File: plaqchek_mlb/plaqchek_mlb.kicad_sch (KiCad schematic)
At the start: 26 parts, among them J1 Conn_01x05, J2 Conn_01x04, J3 Conn_01x02, J4 Conn_01x16, J5 Conn_01x04, SW1 SW_SPST, SW2 SW_Push, SW3 SW_Push, U1 DHT11

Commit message: finish schematic
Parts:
- removed J1: Conn_01x05, symbol Connector_Generic:Conn_01x05
- added C2: 0.1uF, symbol Device:C_Small
- added C3: 10uF, symbol Device:C_Small
- added D1, D2, D3: LED, symbol Device:LED
- added J1: Conn_01x04, symbol Connector_Generic:Conn_01x04
- added R11, R12, R9: 330R, symbol Device:R_Small_US
- R1, R2, R3: value 0 -> 0R
- R10, R33, R34, R8: value 10k -> 10kR
- R31, R7: value 1kΩ -> 1kR
- R4, R5, R6: value 0Ω -> 0R
- U1: value DHT11 -> DHT22
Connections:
- net UNUSED_D2 is gone; now on net UNUSED_D4: J4.5 (Pin_5)
- net UNUSED_D6 is gone; now on net UNUSED_A3: J4.8 (Pin_8)
- net +12V: now also C1.1
- net +3V3: now also C2.1, C3.1; no longer C1.1
- net GND: now also J4.14 (Pin_14), J4.15 (Pin_15), C2.2, C3.2, D1.1 (K), D2.1 (K), D3.1 (K), J1.4 (Pin_4)
- net LED1: now also R9.2
- net LED2: now also R11.2
- net LED3: now also R12.2
- net SPI_5V_ADC_CS: now also J1.1 (Pin_1)
- net SPI_5V_ADC_MISO: now also J1.2 (Pin_2)
- net SPI_5V_ADC_SCLK: now also J1.3 (Pin_3)
- net UNUSED_A3: no longer J4.10 (Pin_10)
- net UNUSED_A6: now also J4.9 (Pin_9); no longer J4.11 (Pin_11)
- net UNUSED_A7: now also J4.10 (Pin_10); no longer J4.12 (Pin_12)
- net UNUSED_AREF: now also J4.11 (Pin_11); no longer J4.13 (Pin_13)
- net UNUSED_D11: now also J4.7 (Pin_7); no longer J4.9 (Pin_9)
- net UNUSED_D4: no longer J4.6 (Pin_6)
- net UNUSED_D5: now also J4.6 (Pin_6); no longer J4.7 (Pin_7)
- net UNUSED_RESET_L_1: now also J4.12 (Pin_12); no longer J4.14 (Pin_14)
- net UNUSED_RESET_L_2: now also J4.13 (Pin_13); no longer J4.15 (Pin_15)
- new net: D2.2 (A), R11.1
- new net: D3.2 (A), R12.1
- new net: D1.2 (A), R9.1
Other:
- moved on the sheet: C1, U1

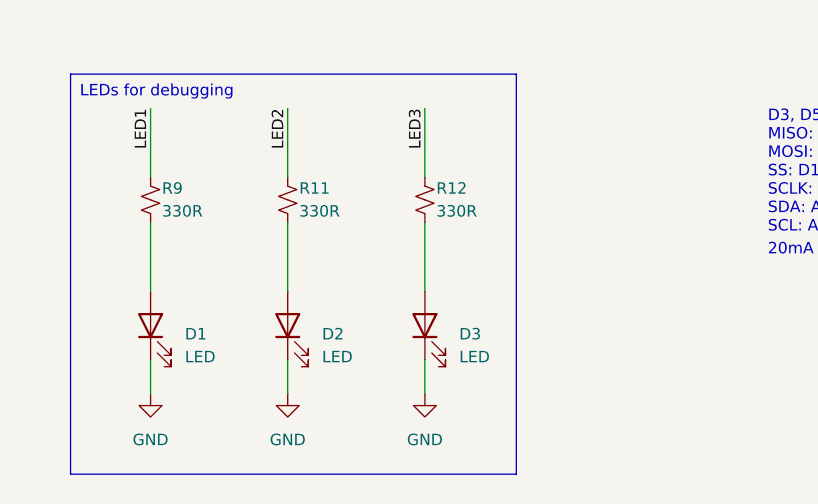
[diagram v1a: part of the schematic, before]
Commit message: more footprints and some value fixes
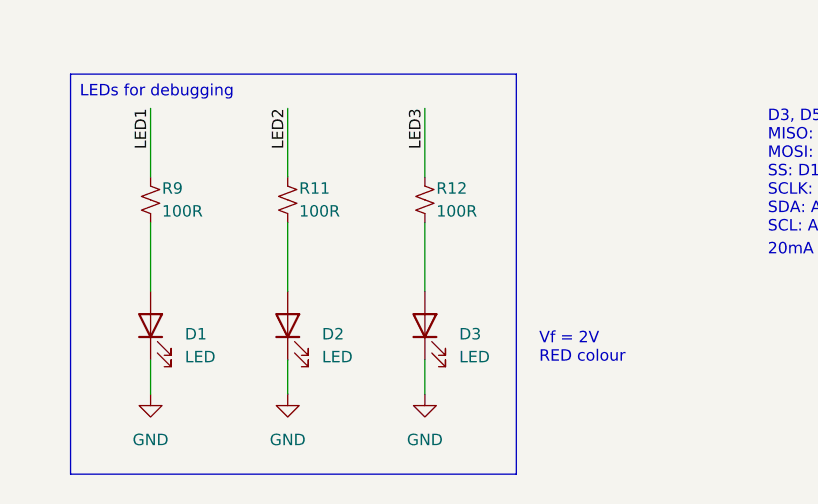
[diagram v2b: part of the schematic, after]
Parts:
- C1, C2, C3, C4, C5: footprint (none) -> Capacitor_SMD:C_0603_1608Metric_Pad1.08x0.95mm_HandSolder
- D1, D2, D3: footprint (none) -> LED_SMD:LED_0805_2012Metric_Pad1.15x1.40mm_HandSolder
- J1, J2, J5: footprint (none) -> Connector_PinHeader_2.54mm:PinHeader_1x04_P2.54mm_Vertical
- J3, JP1: footprint (none) -> Connector_PinHeader_2.54mm:PinHeader_1x02_P2.54mm_Vertical
- J4: footprint (none) -> Connector_PinHeader_2.54mm:PinHeader_1x16_P2.54mm_Vertical
- R1, R10, R2, R3, R31, R33, R34, R4, R5, R6, R7, R8: footprint (none) -> Resistor_SMD:R_0201_0603Metric_Pad0.64x0.40mm_HandSolder
- R11, R12, R9: value 330R -> 100R; footprint (none) -> Resistor_SMD:R_0201_0603Metric_Pad0.64x0.40mm_HandSolder
- SW1, SW2, SW3: footprint (none) -> Button_Switch_THT:SW_PUSH_6mm_H13mm
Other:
- note added: "Vf = 2V RED colour"
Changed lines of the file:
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@@
+    (effects (font (size 1.27 1.27)) (justify left bottom))
+  )
+  (text "Vf = 2V\nRED colour\n\n" (at 73.66 182.88 0)
     (effects (font (size 1.27 1.27)) (justify left bottom))
   )
@@
       (effects (font (size 1.27 1.27)) (justify left))
     )
-    (property "Footprint" "" (at 83.82 39.37 0)
+    (property "Footprint" "Capacitor_SMD:C_0603_1608Metric_Pad1.08x0.95mm_HandSolder" (at 83.82 39.37 0)
       (effects (font (size 1.27 1.27)) hide)
     )
@@
       (effects (font (size 1.27 1.27)))
     )
-    (property "Footprint" "" (at 63.5 72.39 0)
+    (property "Footprint" "Connector_PinHeader_2.54mm:PinHeader_1x02_P2.54mm_Vertical" (at 63.5 72.39 0)
       (effects (font (size 1.27 1.27)) hide)
     )
@@
       (effects (font (size 1.27 1.27)) (justify left))
     )
-    (property "Footprint" "" (at 232.41 144.78 0)
+    (property "Footprint" "Connector_PinHeader_2.54mm:PinHeader_1x04_P2.54mm_Vertical" (at 232.41 144.78 0)
       (effects (font (size 1.27 1.27)) hide)
     )
@@
       (effects (font (size 1.27 1.27)) (justify left))
     )
-    (property "Footprint" "" (at 167.64 30.48 0)
+    (property "Footprint" "Button_Switch_THT:SW_PUSH_6mm_H13mm" (at 167.64 30.48 0)
       (effects (font (size 1.27 1.27)) hide)
     )
@@
       (effects (font (size 1.27 1.27)) (justify right))
     )
-    (property "Value" "330R" (at 46.99 163.83 0)
-      (effects (font (size 1.27 1.27)) (justify right))
-    )
-    (property "Footprint" "" (at 45.72 162.56 0)
+    (property "Value" "100R" (at 46.99 163.83 0)
+      (effects (font (size 1.27 1.27)) (justify right))
+    )
+    (property "Footprint" "Resistor_SMD:R_0201_0603Metric_Pad0.64x0.40mm_HandSolder" (at 45.72 162.56 0)
       (effects (font (size 1.27 1.27)) hide)
     )
@@
       (effects (font (size 1.27 1.27)) (justify right))
     )
-    (property "Footprint" "" (at 194.31 138.43 0)
+    (property "Footprint" "Resistor_SMD:R_0201_0603Metric_Pad0.64x0.40mm_HandSolder" (at 194.31 138.43 0)
       (effects (font (size 1.27 1.27)) hide)
     )
@@
       (effects (font (size 1.27 1.27)) (justify left))
     )
-    (property "Footprint" "" (at 72.39 39.37 0)
+    (property "Footprint" "Capacitor_SMD:C_0603_1608Metric_Pad1.08x0.95mm_HandSolder" (at 72.39 39.37 0)
       (effects (font (size 1.27 1.27)) hide)
     )
@@
       (effects (font (size 1.27 1.27)) (justify right))
     )
-    (property "Footprint" "" (at 60.96 176.53 0)
+    (property "Footprint" "LED_SMD:LED_0805_2012Metric_Pad1.15x1.40mm_HandSolder" (at 60.96 176.53 0)
       (effects (font (size 1.27 1.27)) hide)
     )
@@
       (effects (font (size 1.27 1.27)) (justify right))
     )
-    (property "Footprint" "" (at 41.91 99.06 0)
+    (property "Footprint" "Resistor_SMD:R_0201_0603Metric_Pad0.64x0.40mm_HandSolder" (at 41.91 99.06 0)
       (effects (font (size 1.27 1.27)) hide)
     )
@@
       (effects (font (size 1.27 1.27)))
     )
-    (property "Footprint" "" (at 204.47 119.38 0)
+    (property "Footprint" "Button_Switch_THT:SW_PUSH_6mm_H13mm" (at 204.47 119.38 0)
       (effects (font (size 1.27 1.27)) hide)
     )
@@
       (effects (font (size 1.27 1.27)) (justify right))
     )
-    (property "Footprint" "" (at 58.42 119.38 0)
+    (property "Footprint" "Resistor_SMD:R_0201_0603Metric_Pad0.64x0.40mm_HandSolder" (at 58.42 119.38 0)
       (effects (font (size 1.27 1.27)) hide)
     )
@@
       (effects (font (size 1.27 1.27)) (justify right))
     )
-    (property "Footprint" "" (at 181.61 119.38 0)
+    (property "Footprint" "Resistor_SMD:R_0201_0603Metric_Pad0.64x0.40mm_HandSolder" (at 181.61 119.38 0)
       (effects (font (size 1.27 1.27)) hide)
     )
@@
       (effects (font (size 1.27 1.27)) (justify right))
     )
-    (property "Footprint" "" (at 161.29 116.84 0)
+    (property "Footprint" "Resistor_SMD:R_0201_0603Metric_Pad0.64x0.40mm_HandSolder" (at 161.29 116.84 0)
       (effects (font (size 1.27 1.27)) hide)
     )
@@
       (effects (font (size 1.27 1.27)))
     )
-    (property "Footprint" "" (at 33.02 39.37 0)
+    (property "Footprint" "Connector_PinHeader_2.54mm:PinHeader_1x04_P2.54mm_Vertical" (at 33.02 39.37 0)
       (effects (font (size 1.27 1.27)) hide)
     )
@@
       (effects (font (size 1.27 1.27)) (justify right))
     )
-    (property "Footprint" "" (at 81.28 132.08 0)
+    (property "Footprint" "Resistor_SMD:R_0201_0603Metric_Pad0.64x0.40mm_HandSolder" (at 81.28 132.08 0)
       (effects (font (size 1.27 1.27)) hide)
     )
@@
       (effects (font (size 1.27 1.27)) (justify right))
     )
-    (property "Footprint" "" (at 162.56 41.91 0)
+    (property "Footprint" "Resistor_SMD:R_0201_0603Metric_Pad0.64x0.40mm_HandSolder" (at 162.56 41.91 0)
       (effects (font (size 1.27 1.27)) hide)
     )
@@
       (effects (font (size 1.27 1.27)) (justify right))
     )
-    (property "Value" "330R" (at 62.23 163.83 0)
-      (effects (font (size 1.27 1.27)) (justify right))
-    )
-    (property "Footprint" "" (at 60.96 162.56 0)
+    (property "Value" "100R" (at 62.23 163.83 0)
+      (effects (font (size 1.27 1.27)) (justify right))
+    )
+    (property "Footprint" "Resistor_SMD:R_0201_0603Metric_Pad0.64x0.40mm_HandSolder" (at 60.96 162.56 0)
       (effects (font (size 1.27 1.27)) hide)
     )
@@
       (effects (font (size 1.27 1.27)) (justify left))
     )
-    (property "Footprint" "" (at 71.12 80.01 0)
+    (property "Footprint" "Capacitor_SMD:C_0603_1608Metric_Pad1.08x0.95mm_HandSolder" (at 71.12 80.01 0)
       (effects (font (size 1.27 1.27)) hide)
     )
@@
       (effects (font (size 1.27 1.27)) (justify left))
     )
-    (property "Footprint" "" (at 190.5 30.48 0)
+    (property "Footprint" "Button_Switch_THT:SW_PUSH_6mm_H13mm" (at 190.5 30.48 0)
       (effects (font (size 1.27 1.27)) hide)
     )
@@
       (effects (font (size 1.27 1.27)) (justify left))
     )
-    (property "Footprint" "" (at 80.01 80.01 0)
+    (property "Footprint" "Capacitor_SMD:C_0603_1608Metric_Pad1.08x0.95mm_HandSolder" (at 80.01 80.01 0)
       (effects (font (size 1.27 1.27)) hide)
     )
@@
       (effects (font (size 1.27 1.27)) (justify right))
     )
-    (property "Value" "330R" (at 31.75 163.83 0)
-      (effects (font (size 1.27 1.27)) (justify right))
-    )
-    (property "Footprint" "" (at 30.48 162.56 0)
+    (property "Value" "100R" (at 31.75 163.83 0)
+      (effects (font (size 1.27 1.27)) (justify right))
+    )
+    (property "Footprint" "Resistor_SMD:R_0201_0603Metric_Pad0.64x0.40mm_HandSolder" (at 30.48 162.56 0)
       (effects (font (size 1.27 1.27)) hide)
     )
@@
       (effects (font (size 1.27 1.27)))
     )
-    (property "Footprint" "" (at 236.22 57.15 0)
+    (property "Footprint" "Connector_PinHeader_2.54mm:PinHeader_1x02_P2.54mm_Vertical" (at 236.22 57.15 0)
       (effects (font (size 1.27 1.27)) hide)
     )
@@
       (effects (font (size 1.27 1.27)))
     )
-    (property "Footprint" "" (at 238.76 27.94 0)
+    (property "Footprint" "Connector_PinHeader_2.54mm:PinHeader_1x04_P2.54mm_Vertical" (at 238.76 27.94 0)
       (effects (font (size 1.27 1.27)) hide)
     )
@@
       (effects (font (size 1.27 1.27)))
     )
-    (property "Footprint" "" (at 233.68 99.06 0)
+    (property "Footprint" "Connector_PinHeader_2.54mm:PinHeader_1x16_P2.54mm_Vertical" (at 233.68 99.06 0)
       (effects (font (size 1.27 1.27)) hide)
     )
@@
       (effects (font (size 1.27 1.27)) (justify left))
     )
-    (property "Footprint" "" (at 27.94 86.36 0)
+    (property "Footprint" "Capacitor_SMD:C_0603_1608Metric_Pad1.08x0.95mm_HandSolder" (at 27.94 86.36 0)
       (effects (font (size 1.27 1.27)) hide)
     )
@@
       (effects (font (size 1.27 1.27)) (justify right))
     )
-    (property "Footprint" "" (at 205.74 135.89 0)
+    (property "Footprint" "Resistor_SMD:R_0201_0603Metric_Pad0.64x0.40mm_HandSolder" (at 205.74 135.89 0)
       (effects (font (size 1.27 1.27)) hide)
     )
@@
       (effects (font (size 1.27 1.27)) (justify right))
     )
-    (property "Footprint" "" (at 45.72 176.53 0)
+    (property "Footprint" "LED_SMD:LED_0805_2012Metric_Pad1.15x1.40mm_HandSolder" (at 45.72 176.53 0)
       (effects (font (size 1.27 1.27)) hide)
     )
@@
       (effects (font (size 1.27 1.27)) (justify right))
     )
-    (property "Footprint" "" (at 185.42 41.91 0)
+    (property "Footprint" "Resistor_SMD:R_0201_0603Metric_Pad0.64x0.40mm_HandSolder" (at 185.42 41.91 0)
       (effects (font (size 1.27 1.27)) hide)
     )
@@
       (effects (font (size 1.27 1.27)) (justify right))
     )
-    (property "Footprint" "" (at 30.48 176.53 0)
+    (property "Footprint" "LED_SMD:LED_0805_2012Metric_Pad1.15x1.40mm_HandSolder" (at 30.48 176.53 0)
       (effects (font (size 1.27 1.27)) hide)
     )
@@
       (effects (font (size 1.27 1.27)) (justify right))
     )
-    (property "Footprint" "" (at 81.28 124.46 0)
+    (property "Footprint" "Resistor_SMD:R_0201_0603Metric_Pad0.64x0.40mm_HandSolder" (at 81.28 124.46 0)
       (effects (font (size 1.27 1.27)) hide)
     )
@@
       (effects (font (size 1.27 1.27)) (justify right))
     )
-    (property "Footprint" "" (at 81.28 129.54 0)
+    (property "Footprint" "Resistor_SMD:R_0201_0603Metric_Pad0.64x0.40mm_HandSolder" (at 81.28 129.54 0)
       (effects (font (size 1.27 1.27)) hide)
     )
@@
       (effects (font (size 1.27 1.27)) (justify right))
     )
-    (property "Footprint" "" (at 140.97 114.3 0)
-      (effects (font (size 1.27 1.27)) hide)
-    )
+    (property "Footprint" "Resistor_SMD:R_0201_0603Metric_Pad0.64x0.40mm_HandSolder" (at 140.97 114.3 0)
+      (effects (font (size 1.27 1.27)) hide)
+    )

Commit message: finish main logic board PCB routing
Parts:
- removed J4: Conn_01x16, Connector_PinHeader_2.54mm:PinHeader_1x16_P2.54mm_Vertical, symbol Connector_Generic:Conn_01x16
- removed SW1: SW_SPST, Button_Switch_THT:SW_PUSH_6mm_H13mm, symbol Switch:SW_SPST
- added H1, H2, H3, H4: MountingHole_Pad, MountingHole:MountingHole_3.2mm_M3_Pad, symbol Mechanical:MountingHole_Pad
- added R1 (x4): 0R, Resistor_SMD:R_0603_1608Metric_Pad0.98x0.95mm_HandSolder, symbol Device:R_Small_US
- added R13: 10kR, Resistor_SMD:R_0603_1608Metric_Pad0.98x0.95mm_HandSolder, symbol Device:R_Small_US
- added SW1: SW_Push, Button_Switch_THT:SW_PUSH_6mm_H13mm, symbol Switch:SW_Push
- added TP1, TP2, TP3, TP4: TestPoint, TestPoint:TestPoint_Pad_D1.0mm, symbol Connector:TestPoint
- R1, R10, R11, R12, R2, R3, R31, R33, R34, R4, R5, R6, R7, R8, R9: footprint Resistor_SMD:R_0201_0603Metric_Pad0.64x0.40mm_HandSolder -> Resistor_SMD:R_0603_1608Metric_Pad0.98x0.95mm_HandSolder
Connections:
- net UNUSED_A7 is gone; now on net PD_EN: A1.26 (A7)
- net +3V3: now also SW1.1
- net GND: now also R1.2, R1.2, R1.2, R1.2, R13.1, TP1.1, TP2.1, TP3.1, TP4.1
- net PD_EN: no longer A1.9 (D6)
- net SW_FLIP_R: now also R13.2, SW1.2
- net SPI_5V_ADC_CS renamed SPI_3V3_ADC_CS
- net SPI_5V_ADC_MISO renamed SPI_3V3_ADC_MISO
- net SPI_5V_ADC_SCLK renamed SPI_3V3_ADC_SCLK
- net UNUSED_3V3: no longer names the net of A1.17 (3V3)
- net UNUSED_5V: no longer names the net of A1.27 (+5V)
- net UNUSED_A3: no longer names the net of A1.22 (A3)
- net UNUSED_A6: no longer names the net of A1.25 (A6)
- net UNUSED_AREF: no longer names the net of A1.18 (AREF)
- net UNUSED_D0/RX: no longer names the net of A1.2 (D0/RX)
- net UNUSED_D11: no longer names the net of A1.14 (D11)
- net UNUSED_D1/TX: no longer names the net of A1.1 (D1/TX)
- net UNUSED_D4: no longer names the net of A1.7 (D4)
- net UNUSED_D5: no longer names the net of A1.8 (D5)
- net UNUSED_RESET_L_1: no longer names the net of A1.28 (~{RESET})
- net UNUSED_RESET_L_2: no longer names the net of A1.3 (~{RESET})
- net VDAC_POT_PWM_5V renamed VDAC_POT_PWM_3V3
- new net: H3.1, R1.1
- new net: H2.1, R1.1
- new net: H1.1, R1.1
- new net: H4.1, R1.1
- no-connect marks 0 -> 13
